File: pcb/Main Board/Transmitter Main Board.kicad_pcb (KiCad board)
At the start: 2 copper layers, 96.5 x 96.5 mm, 36 parts, among them J1 Battery, J2 BATTERY MONITOR, J3 Throttle, J4 Steering, J5 VR3, J6 XY JOYSTICK, SW1 SW_Push, SW2 SW_Push, SW3 SW_Push, SW4 SW_Push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

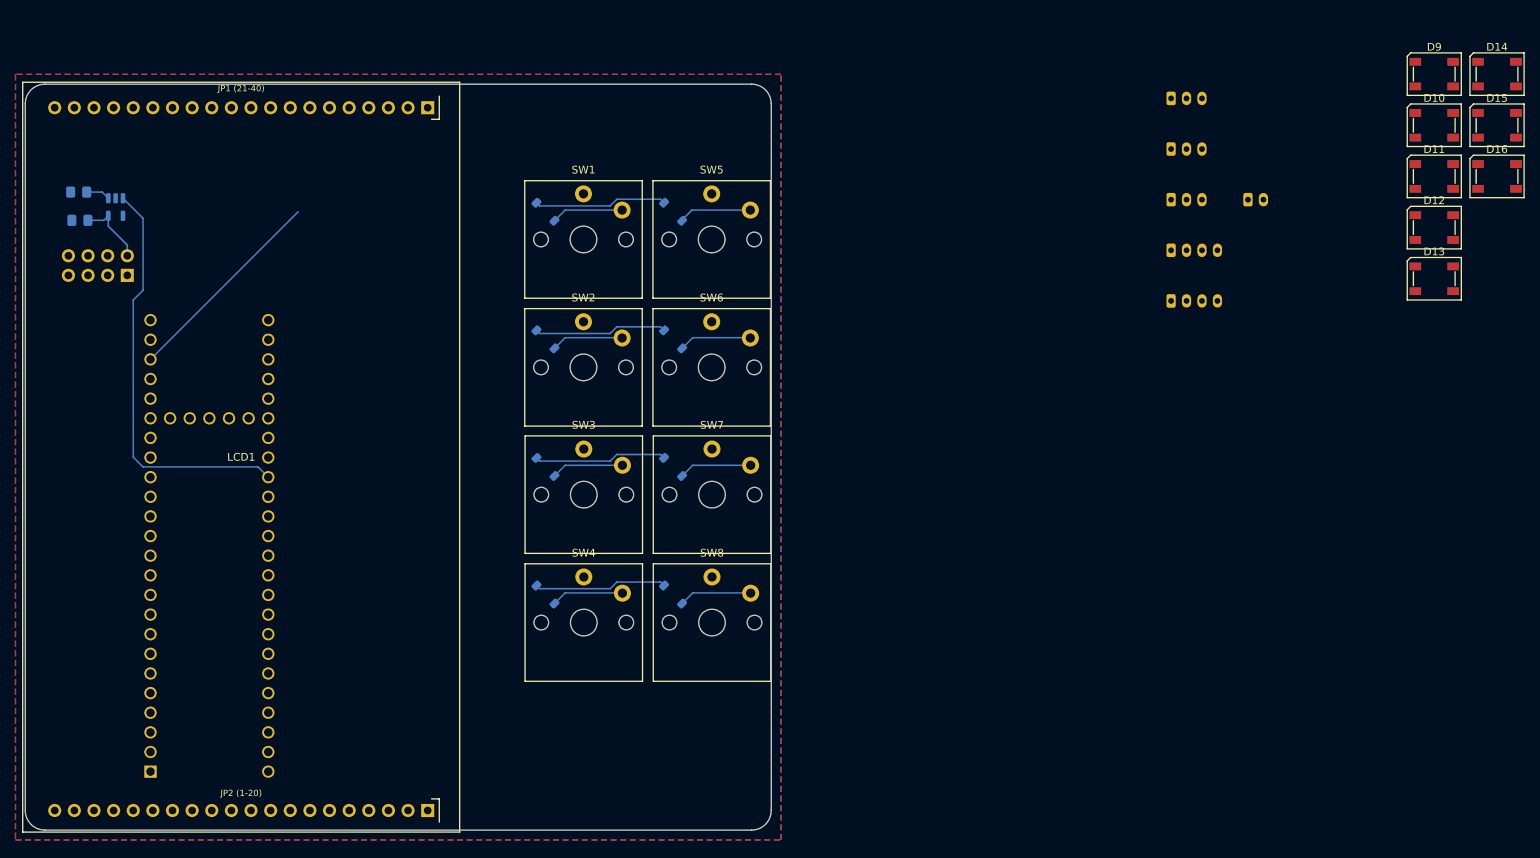
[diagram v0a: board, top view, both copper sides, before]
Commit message: Create 4960 symbol and footprint
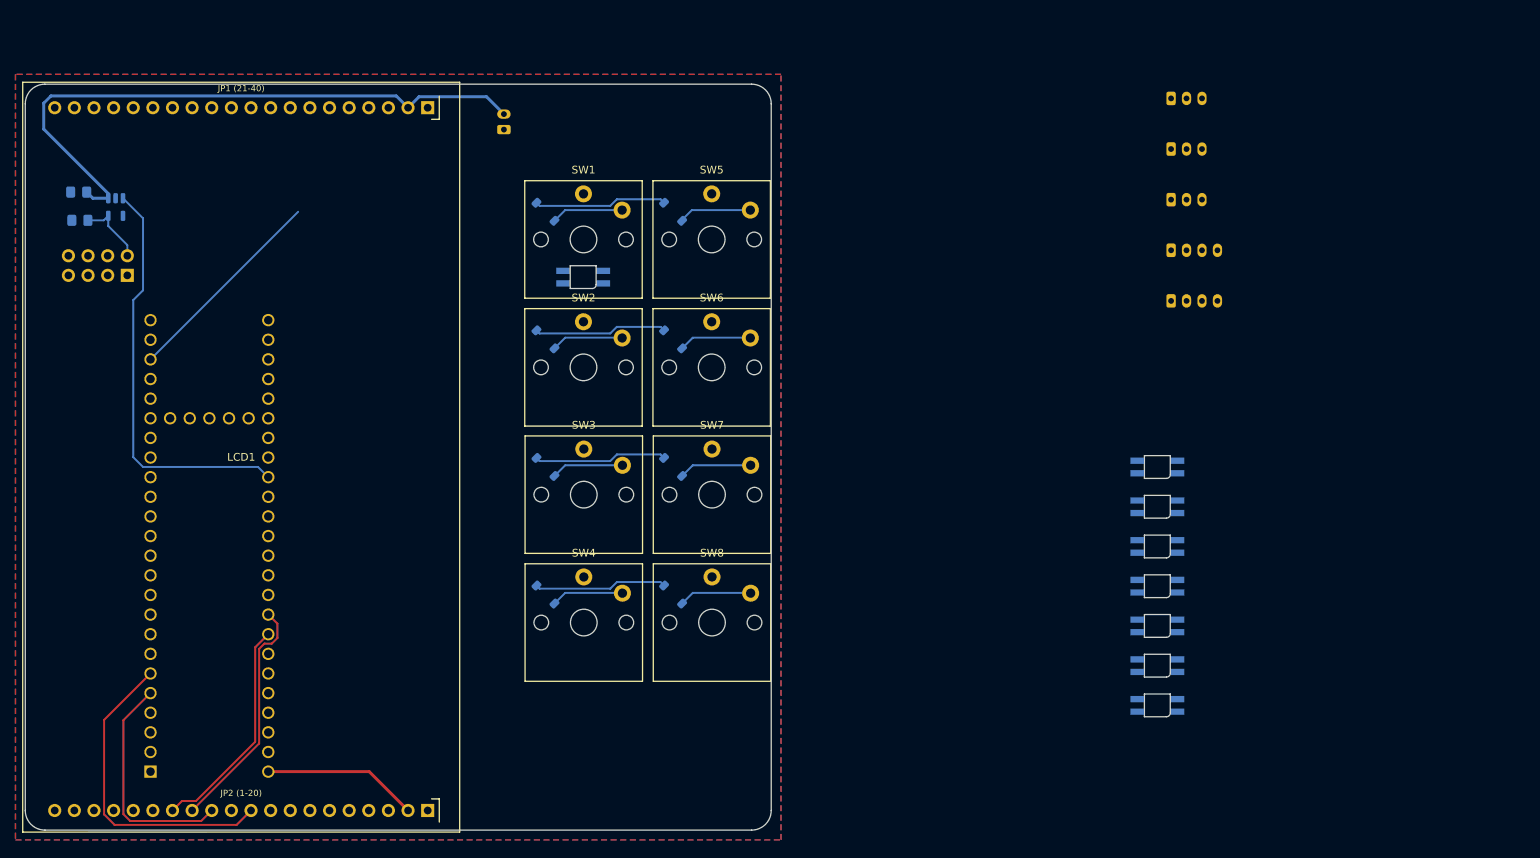
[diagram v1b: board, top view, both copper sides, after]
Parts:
- removed D10, D11, D12, D13, D14, D15, D16, D9: SK6812, LED_SMD:LED_SK6812_PLCC4_5.0x5.0mm_P3.2mm
- added IC1: 4960, Transmitter Library:4960_ADA, F.Cu at (112.8, 80.8)
- added IC2: 4960, Transmitter Library:4960_ADA, F.Cu at (187.1, 105.4)
- added IC3: 4960, Transmitter Library:4960_ADA, F.Cu at (187.1, 110.6)
- added IC4: 4960, Transmitter Library:4960_ADA, F.Cu at (187.1, 115.7)
- added IC5: 4960, Transmitter Library:4960_ADA, F.Cu at (187.1, 120.8)
- added IC6: 4960, Transmitter Library:4960_ADA, F.Cu at (187.1, 126.0)
- added IC7: 4960, Transmitter Library:4960_ADA, F.Cu at (187.1, 131.1)
- added IC8: 4960, Transmitter Library:4960_ADA, F.Cu at (187.1, 136.3)
- moved J1 96.7 mm to (102.6, 61.8), turned to 90 degrees
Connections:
- J1 pad 1: +BATT -> GND
- J1 pad 2: GND -> +BATT
- U1 pad 5: /BACKLIGHT -> /TFT_IRQ
- U1 pad 6: /TFT_IRQ -> /BACKLIGHT
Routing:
- net +BATT: track 3.13 -> 101.1 mm
- net /BACKLIGHT: track 0.00 -> 41.1 mm
- net SDA: track 0.00 -> 31.3 mm
- net /TFT_IRQ: track 0.00 -> 29.5 mm
- net SCL: track 0.00 -> 29.0 mm

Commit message: more routing
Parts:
- added J7: Neopixel Out, Connector_JST:JST_PH_B3B-PH-K_1x03_P2.00mm_Vertical, B.Cu at (110.7, 65.2)
- moved J5 146.0 mm to (59.7, 125.7)
- moved J4 140.5 mm to (59.7, 119.4)
- moved J3 135.9 mm to (59.7, 113.0)
- moved J6 132.5 mm to (59.7, 106.7)
- moved J2 130.2 mm to (59.7, 100.3)
- moved IC4 77.1 mm to (112.9, 136.6)
- moved IC8 75.8 mm to (129.5, 87.0), turned to 180 degrees
- moved IC3 74.8 mm to (112.9, 120.0)
- moved IC2 74.3 mm to (112.9, 103.6), turned to 180 degrees
- moved IC7 63.9 mm to (129.5, 103.6), turned to 180 degrees
- moved IC5 59.7 mm to (129.5, 136.6), turned to 180 degrees
- moved IC6 57.9 mm to (129.5, 120.0), turned to 180 degrees
- moved J1 50.6 mm to (63.5, 94.0), turned to 0 degrees
- moved U1 21.6 mm to (83.5, 105.5), turned to -90 degrees
- moved C1 14.7 mm to (61.5, 74.5), turned to 90 degrees
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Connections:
- J2 pad 2: GND -> SCL1
- J2 pad 3: SCL1 -> SDA1
- J2 pad 4: SDA1 -> GND
- J3 pad 1: GND -> +3.3V
- J3 pad 3: +3.3V -> GND
- J4 pad 1: GND -> +3.3V
- J4 pad 3: +3.3V -> GND
- J5 pad 1: GND -> +3.3V
- J5 pad 3: +3.3V -> GND
- J6 pad 1: GND -> +3.3V
- J6 pad 4: +3.3V -> GND
- LCD1 pad 22: +BATT -> unconnected-(LCD1-VIN-Pad22)
- U1 pad 20: unconnected-(U1-28_RX7-Pad20) -> /ROW_1
- U1 pad 21: unconnected-(U1-29_TX7-Pad21) -> /ROW_2
- U1 pad 22: /ROW_1 -> /ROW_3
- U1 pad 23: /ROW_2 -> /ROW_4
- U1 pad 24: /ROW_3 -> unconnected-(U1-32_OUT1B-Pad24)
- U1 pad 25: /ROW_4 -> /COL_B
- U1 pad 27: /COL_B -> unconnected-(U1-35_TX8-Pad27)
- U1 pad 40: SDA -> SCL
- U1 pad 41: SCL -> SDA
- U1 pad 42: /VR1 -> /VR3
- U1 pad 44: /VR3 -> /VR1
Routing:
- net +3.3V: track 0.00 -> 215.9 mm, vias 0 -> 4
- net /COL_B: track 0.00 -> 117.0 mm, vias 0 -> 1
- net /COL_A: track 0.00 -> 103.5 mm
- net SCK: track 0.00 -> 86.0 mm
- net /BACKLIGHT: track 41.1 -> 0.00 mm
- net /VR3: track 0.00 -> 40.1 mm
- net /ROW_2: track 17.2 -> 56.7 mm
- net Net-(IC1-DOUT): track 0.00 -> 37.1 mm
- net +BATT: track 101.1 -> 64.7 mm
- net /VR2: track 0.00 -> 36.3 mm
- net /VR1: track 0.00 -> 32.5 mm
- net /2x8 Button Matrix/NEO_OUT: track 0.00 -> 30.3 mm
- net /TFT_IRQ: track 29.5 -> 0.00 mm
- net /ROW_1: track 44.2 -> 70.6 mm, vias 0 -> 1
- net /ROW_3: track 17.2 -> 42.7 mm
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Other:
- board text added: "Micro SD"

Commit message: more more more routing
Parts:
- added J8: Neopixel Out, Connector_JST:JST_PH_B3B-PH-K_1x03_P2.00mm_Vertical, B.Cu at (120.7, 64.8)
- J3: value Throttle -> i2c; footprint Connector_JST:JST_PH_B3B-PH-K_1x03_P2.00mm_Vertical -> Connector_JST:JST_PH_B4B-PH-K_1x04_P2.00mm_Vertical
- J4: value Steering -> Throttle
- J5: value VR3 -> Steering
- J6: value XY JOYSTICK -> VR3; footprint Connector_JST:JST_PH_B4B-PH-K_1x04_P2.00mm_Vertical -> Connector_JST:JST_PH_B3B-PH-K_1x03_P2.00mm_Vertical
- J7: value Neopixel Out -> XY JOYSTICK; footprint Connector_JST:JST_PH_B3B-PH-K_1x03_P2.00mm_Vertical -> Connector_JST:JST_PH_B4B-PH-K_1x04_P2.00mm_Vertical
- moved J7 57.0 mm to (62.2, 95.2)
- moved J3 24.3 mm to (62.2, 88.9)
- moved J1 18.0 mm to (66.0, 76.2)
- moved J2 18.0 mm to (62.2, 82.5)
- moved J5 18.0 mm to (62.2, 108.0)
- moved U3 7.30 mm to (55.9, 87.6)
- moved J6 5.68 mm to (62.2, 101.6)
- moved J4 5.68 mm to (62.2, 114.3)
- moved IC4 5.44 mm to (109.2, 140.6), turned to 180 degrees
- moved SW4 5.44 mm to (109.2, 135.9)
- moved IC1 5.11 mm to (109.2, 83.4)
- moved SW1 5.11 mm to (109.2, 78.7)
- moved U2 5.08 mm to (59.5, 74.2)
- moved C2 4.78 mm to (57.7, 69.8)
- moved C1 4.62 mm to (61.5, 69.8)
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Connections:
- IC5 pad 2: Net-(IC5-DOUT) -> /2x8 Button Matrix/NEO_OUT
- IC5 pad 4: Net-(IC4-DOUT) -> Net-(IC5-DIN)
- IC6 pad 2: Net-(IC6-DOUT) -> Net-(IC5-DIN)
- IC6 pad 4: Net-(IC5-DOUT) -> Net-(IC6-DIN)
- IC7 pad 2: Net-(IC7-DOUT) -> Net-(IC6-DIN)
- IC7 pad 4: Net-(IC6-DOUT) -> Net-(IC7-DIN)
- IC8 pad 2: /2x8 Button Matrix/NEO_OUT -> Net-(IC7-DIN)
- IC8 pad 4: Net-(IC7-DOUT) -> Net-(IC4-DOUT)
- J1 pad 1: GND -> +BATT
- J1 pad 2: +BATT -> GND
- J3 pad 2: /VR1 -> SCL1
- J3 pad 3: GND -> SDA1
- J4 pad 2: /VR2 -> /VR1
- J5 pad 2: /VR3 -> /VR2
- J6 pad 2: /JOY_X -> /VR3
- J6 pad 3: /JOY_Y -> GND
- J7 pad 2: /2x8 Button Matrix/NEO_OUT -> /JOY_X
- J7 pad 3: GND -> /JOY_Y
- U1 pad 20: /ROW_1 -> unconnected-(U1-28_RX7-Pad20)
- U1 pad 21: /ROW_2 -> unconnected-(U1-29_TX7-Pad21)
- U1 pad 4: /TFT_D/C -> /TFT_IRQ
- U1 pad 5: /TFT_IRQ -> /BACKLIGHT
- U1 pad 6: /BACKLIGHT -> /TFT_D/C
- U1 pad 7: /NEOPIXEL -> /ROW_1
- U1 pad 8: unconnected-(U1-6_OUT1D-Pad8) -> /NEOPIXEL
- U1 pad 9: unconnected-(U1-7_RX2_OUT1A-Pad9) -> /ROW_2
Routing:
- net SCK1: track 0.00 -> 102.7 mm
- net MOSI1: track 0.00 -> 101.0 mm
- net MOSI: track 0.00 -> 73.2 mm
- net /RF_CS: track 0.00 -> 72.2 mm
- net /RF_CE: track 0.00 -> 69.8 mm
- net MISO: track 0.00 -> 69.4 mm
- net MISO1: track 0.00 -> 65.8 mm
- net /TFT_D/C: track 0.00 -> 46.5 mm
- net /TFT_CS: track 0.00 -> 43.0 mm
- net /BACKLIGHT: track 0.00 -> 39.3 mm
- net /JOY_Y: track 13.2 -> 50.7 mm
- net Net-(IC1-DOUT): track 37.1 -> 0.00 mm
- net +3.3V: track 215.9 -> 251.6 mm, vias 4 -> 8
- net /JOY_X: track 15.4 -> 49.0 mm
- net SCK: track 86.0 -> 52.5 mm
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
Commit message: finalish routing
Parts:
- added J10: Neopixel Out, Connector_JST:JST_PH_B3B-PH-K_1x03_P2.00mm_Vertical, B.Cu at (120.7, 64.8)
- added J9: UART7, Connector_JST:JST_PH_B4B-PH-K_1x04_P2.00mm_Vertical, B.Cu at (62.2, 128.3)
- J4: value Throttle -> XY JOYSTICK; footprint Connector_JST:JST_PH_B3B-PH-K_1x03_P2.00mm_Vertical -> Connector_JST:JST_PH_B4B-PH-K_1x04_P2.00mm_Vertical
- J5: value Steering -> VR3
- J6: value VR3 -> Steering
- J7: value XY JOYSTICK -> Throttle; footprint Connector_JST:JST_PH_B4B-PH-K_1x04_P2.00mm_Vertical -> Connector_JST:JST_PH_B3B-PH-K_1x03_P2.00mm_Vertical
- J8: value Neopixel Out -> UART6/i2c2; footprint Connector_JST:JST_PH_B3B-PH-K_1x03_P2.00mm_Vertical -> Connector_JST:JST_PH_B4B-PH-K_1x04_P2.00mm_Vertical
- moved J8 81.7 mm to (62.2, 121.9)
- moved IC5 57.2 mm to (128.3, 83.4)
- moved IC8 57.2 mm to (128.3, 140.6)
- moved IC6 19.1 mm to (128.3, 102.5)
- moved IC7 19.1 mm to (128.3, 121.5)
- moved J4 19.0 mm to (62.2, 95.2)
- moved J7 19.0 mm to (62.2, 114.3)
- moved C2 12.4 mm to (52.6, 81.2), turned to 180 degrees
- moved C1 11.7 mm to (52.6, 77.4), turned to 180 degrees
- moved D8 8.32 mm to (117.3, 127.8), turned to 0 degrees
- moved D7 8.32 mm to (117.3, 108.7), turned to 0 degrees
- moved D6 8.19 mm to (117.3, 89.9), turned to 0 degrees
- moved J5 6.35 mm to (62.2, 101.6)
- moved J6 6.35 mm to (62.2, 108.0)
- moved U2 5.77 mm to (56.9, 79.3), turned to -90 degrees
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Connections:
- net Net-(U2-OUT) renamed /RF_PWR
- J4 pad 2: /VR1 -> /JOY_X
- J4 pad 3: GND -> /JOY_Y
- J5 pad 2: /VR2 -> /VR3
- J6 pad 2: /VR3 -> /VR2
- J7 pad 2: /JOY_X -> /VR1
- J7 pad 3: /JOY_Y -> GND
- J8 pad 1: +3.3V -> /3V3
- J8 pad 2: /2x8 Button Matrix/NEO_OUT -> /TX6
- J8 pad 3: GND -> /RX6
- U1 pad 15: unconnected-(U1-3V3-Pad15) -> /3V3
- U1 pad 16: unconnected-(U1-24_A10_TX6_SCL2-Pad16) -> /TX6
- U1 pad 17: unconnected-(U1-25_A11_RX6_SDA2-Pad17) -> /RX6
- U1 pad 20: unconnected-(U1-28_RX7-Pad20) -> /RX7
- U1 pad 21: unconnected-(U1-29_TX7-Pad21) -> /TX7
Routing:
- net /3V3: track 0.00 -> 39.8 mm
- net Net-(IC7-DIN): track 0.00 -> 37.6 mm
- net Net-(IC6-DIN): track 0.00 -> 37.5 mm
- net Net-(IC5-DIN): track 0.00 -> 37.2 mm
- net Net-(IC3-DOUT): track 0.00 -> 35.1 mm
- net Net-(IC2-DOUT): track 0.00 -> 34.8 mm
- net Net-(IC1-DOUT): track 0.00 -> 34.6 mm
- net /TX6: track 0.00 -> 30.4 mm
- net /TX7: track 0.00 -> 29.8 mm
- net Net-(IC4-DOUT): track 0.00 -> 28.4 mm
- net /RX7: track 0.00 -> 27.8 mm
- net /RX6: track 0.00 -> 27.4 mm
- net /2x8 Button Matrix/NEO_OUT: track 0.00 -> 24.8 mm
- net /COL_B: track 117.5 -> 128.7 mm
- net SDA: track 36.1 -> 45.8 mm
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
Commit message: Final final routing
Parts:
- added H1: MountingHole_Pad, MountingHole:MountingHole_3.2mm_M3_Pad, F.Cu at (191.8, 52.1)
- added H2: MountingHole_Pad, MountingHole:MountingHole_3.2mm_M3_Pad, F.Cu at (191.8, 141.0)
- added JP1: SolderJumper_3_Bridged12, Jumper:SolderJumper-3_P2.0mm_Open_TrianglePad1.0x1.5mm, B.Cu at (109.2, 109.2)
- added JP2: SolderJumper_3_Bridged12, Jumper:SolderJumper-3_P2.0mm_Open_TrianglePad1.0x1.5mm, B.Cu at (109.2, 115.6)
- added JP3: SolderJumper_3_Bridged12, Jumper:SolderJumper-3_P2.0mm_Open_TrianglePad1.0x1.5mm, B.Cu at (109.2, 122.2)
- J3: value i2c -> UART4/i2c1
- J4: value XY JOYSTICK -> Aux IO
- J5: value VR3 -> Steering
- J6: value Steering -> Throttle
- J7: value Throttle -> XY Joystick/UART3; footprint Connector_JST:JST_PH_B3B-PH-K_1x03_P2.00mm_Vertical -> Connector_JST:JST_PH_B5B-PH-K_1x05_P2.00mm_Vertical
- J8, J9: footprint Connector_JST:JST_PH_B4B-PH-K_1x04_P2.00mm_Vertical -> Connector_JST:JST_PH_B5B-PH-K_1x05_P2.00mm_Vertical
- moved D1 58.9 mm to (163.8, 67.3)
- moved D2 58.9 mm to (163.8, 86.4)
- moved D3 58.9 mm to (163.8, 105.4)
- moved D4 58.9 mm to (163.8, 124.5)
- moved U1 58.9 mm to (142.2, 97.8)
- moved J1 58.9 mm to (120.7, 68.6)
- moved J2 58.9 mm to (120.7, 74.9)
- moved J3 58.9 mm to (120.7, 81.3)
- moved J4 58.9 mm to (120.7, 87.6)
- moved J5 58.9 mm to (120.7, 94.0)
- moved J6 58.9 mm to (120.7, 100.3)
- moved D6 58.9 mm to (175.8, 82.3)
- moved D7 58.9 mm to (175.8, 101.1)
- moved D8 58.9 mm to (175.8, 120.1)
- moved LCD1 58.9 mm to (127.0, 96.5)
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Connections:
- J4 pad 2: /JOY_X -> /VR4
- J4 pad 3: /JOY_Y -> /VR3
- J5 pad 2: /VR3 -> /VR2
- J6 pad 2: /VR2 -> /VR1
- J7 pad 1: +3.3V -> Net-(J7-Pin_1)
- J7 pad 2: /VR1 -> /BTN
- J7 pad 3: GND -> /JOY_X
- J8 pad 1: /3V3 -> Net-(J8-Pin_1)
- J8 pad 2: /TX6 -> /UART6_AUX
- J8 pad 3: /RX6 -> /TX6
- J8 pad 4: GND -> /RX6
- J9 pad 1: /3V3 -> Net-(J9-Pin_1)
- J9 pad 2: /TX7 -> /UART7_AUX
- J9 pad 3: /RX7 -> /TX7
- J9 pad 4: GND -> /RX7
- U1 pad 11: /RF_CE -> unconnected-(U1-9_OUT1C-Pad11)
- U1 pad 28: unconnected-(U1-36_CS-Pad28) -> /UART7_AUX
- U1 pad 29: unconnected-(U1-37_CS-Pad29) -> /UART6_AUX
- U1 pad 31: unconnected-(U1-39_MISO1_OUT1A-Pad31) -> /BTN
- U1 pad 32: unconnected-(U1-40_A16-Pad32) -> /JOY_X
- U1 pad 33: /RF_EN -> /JOY_Y
- U1 pad 36: /JOY_X -> /RF_CE
- U1 pad 37: /JOY_Y -> /RF_EN
- U1 pad 40: SCL -> SDA
- U1 pad 41: SDA -> SCL
- U1 pad 42: /VR3 -> /VR4
- U1 pad 43: /VR2 -> /VR3
- U1 pad 44: /VR1 -> /VR2
- U1 pad 45: unconnected-(U1-23_A9_CRX1_MCLK1-Pad45) -> /VR1
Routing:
- net +BATT: track 53.3 -> 149.8 mm, vias 0 -> 3
- net /VR4: track 0.00 -> 47.3 mm
- net /JOY_Y: track 49.4 -> 9.02 mm
- net /JOY_X: track 47.7 -> 11.0 mm
- net /RF_CE: track 72.9 -> 44.5 mm
- net MOSI1: track 109.1 -> 87.8 mm
- net /3V3: track 39.8 -> 60.8 mm
- net +3.3V: track 253.2 -> 234.1 mm
- net SCK1: track 107.1 -> 90.4 mm
- net /UART7_AUX: track 0.00 -> 13.0 mm
- net /BTN: track 0.00 -> 13.0 mm
- net /UART6_AUX: track 0.00 -> 12.9 mm
- net Net-(J7-Pin_1): track 0.00 -> 12.3 mm
- net Net-(J8-Pin_1): track 0.00 -> 12.3 mm
- net Net-(J9-Pin_1): track 0.00 -> 12.2 mm
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
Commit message: begin overcomplication
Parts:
- removed J10: Neopixel Out, Connector_JST:JST_PH_B3B-PH-K_1x03_P2.00mm_Vertical
- added JP4: SolderJumper_3_Bridged12, Jumper:SolderJumper-3_P2.0mm_Open_TrianglePad1.0x1.5mm, B.Cu at (109.2, 122.2)
- added R1: R, Resistor_SMD:R_0805_2012Metric_Pad1.20x1.40mm_HandSolder, B.Cu at (127.3, 70.6)
- added R2: R, Resistor_SMD:R_0805_2012Metric_Pad1.20x1.40mm_HandSolder, B.Cu at (129.8, 70.6)
- added R3: R, Resistor_SMD:R_0805_2012Metric_Pad1.20x1.40mm_HandSolder, B.Cu at (140.6, 56.0)
- added R4: R, Resistor_SMD:R_0805_2012Metric_Pad1.20x1.40mm_HandSolder, B.Cu at (138.8, 57.8)
- J2: value BATTERY MONITOR -> UART4/i2c1; footprint Connector_JST:JST_PH_B4B-PH-K_1x04_P2.00mm_Vertical -> Connector_JST:JST_PH_B5B-PH-K_1x05_P2.00mm_Vertical
- J3: value UART4/i2c1 -> Aux IO
- J4: value Aux IO -> Steering; footprint Connector_JST:JST_PH_B4B-PH-K_1x04_P2.00mm_Vertical -> Connector_JST:JST_PH_B3B-PH-K_1x03_P2.00mm_Vertical
- J5: value Steering -> Throttle
- J6: value Throttle -> XY Joystick/UART3; footprint Connector_JST:JST_PH_B3B-PH-K_1x03_P2.00mm_Vertical -> Connector_JST:JST_PH_B5B-PH-K_1x05_P2.00mm_Vertical
- J7: value XY Joystick/UART3 -> UART6/i2c2
- J8: value UART6/i2c2 -> UART7
- J9: value UART7 -> Neopixel Out; footprint Connector_JST:JST_PH_B5B-PH-K_1x05_P2.00mm_Vertical -> Connector_JST:JST_PH_B3B-PH-K_1x03_P2.00mm_Vertical
- moved J9 87.2 mm to (179.1, 57.1)
- moved JP1 37.0 mm to (121.7, 74.4), turned to 180 degrees
- moved J6 8.89 mm to (120.7, 109.2)
- moved JP3 6.60 mm to (109.2, 115.6)
- moved JP2 6.60 mm to (109.2, 109.0)
- moved J4 6.35 mm to (120.7, 94.0)
- moved J8 6.35 mm to (120.7, 121.9)
- moved J2 6.35 mm to (120.7, 81.3)
- moved J3 6.35 mm to (120.7, 87.6)
- moved J5 6.35 mm to (120.7, 100.3)
- moved J7 6.35 mm to (120.7, 115.6)
- moved J1 4.02 mm to (121.9, 64.8), turned to -90 degrees
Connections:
- J2 pad 1: +3.3V -> Net-(J2-Pin_1)
- J2 pad 2: SCL1 -> /i2c1_INT
- J2 pad 3: SDA1 -> SCL1
- J2 pad 4: GND -> SDA1
- J3 pad 2: SCL1 -> /VR4
- J3 pad 3: SDA1 -> /VR3
- J4 pad 2: /VR4 -> /VR2
- J4 pad 3: /VR3 -> GND
- J5 pad 2: /VR2 -> /VR1
- J6 pad 1: +3.3V -> Net-(J6-Pin_1)
- J6 pad 2: /VR1 -> /BTN
- J6 pad 3: GND -> /JOY_X
- J7 pad 2: /BTN -> /UART6_AUX
- J7 pad 3: /JOY_X -> /TX6
- J7 pad 4: /JOY_Y -> /RX6
- J8 pad 2: /UART6_AUX -> /UART7_AUX
- J8 pad 3: /TX6 -> /TX7
- J8 pad 4: /RX6 -> /RX7
- J9 pad 1: Net-(J9-Pin_1) -> +3.3V
- J9 pad 2: /UART7_AUX -> /2x8 Button Matrix/NEO_OUT
- J9 pad 3: /TX7 -> GND
- JP1 pad 1: /3V3 -> +3.3V
- JP1 pad 2: Net-(J7-Pin_1) -> Net-(J2-Pin_1)
- JP2 pad 2: Net-(J8-Pin_1) -> Net-(J6-Pin_1)
- JP3 pad 2: Net-(J9-Pin_1) -> Net-(J7-Pin_1)
- U1 pad 10: unconnected-(U1-8_TX2_IN1-Pad10) -> /i2c1_INT
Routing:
- net /i2c1_INT: track 0.00 -> 36.0 mm
- net +3.3V: track 234.1 -> 248.9 mm, vias 8 -> 10
- net +BATT: track 149.8 -> 164.5 mm
- net Net-(J6-Pin_1): track 0.00 -> 12.3 mm
- net Net-(J9-Pin_1): track 12.2 -> 0.00 mm
- net SDA: track 39.0 -> 47.3 mm
- net Net-(J2-Pin_1): track 0.00 -> 7.28 mm
- net SCL: track 37.1 -> 43.3 mm
- net GND: track 9.99 -> 12.9 mm, vias 21 -> 25
- net SCL1: track 25.6 -> 28.3 mm
- net SDA1: track 22.2 -> 24.9 mm
- net /RF_EN: track 52.3 -> 53.0 mm
